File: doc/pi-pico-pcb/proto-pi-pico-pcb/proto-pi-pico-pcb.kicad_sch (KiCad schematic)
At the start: 10 parts

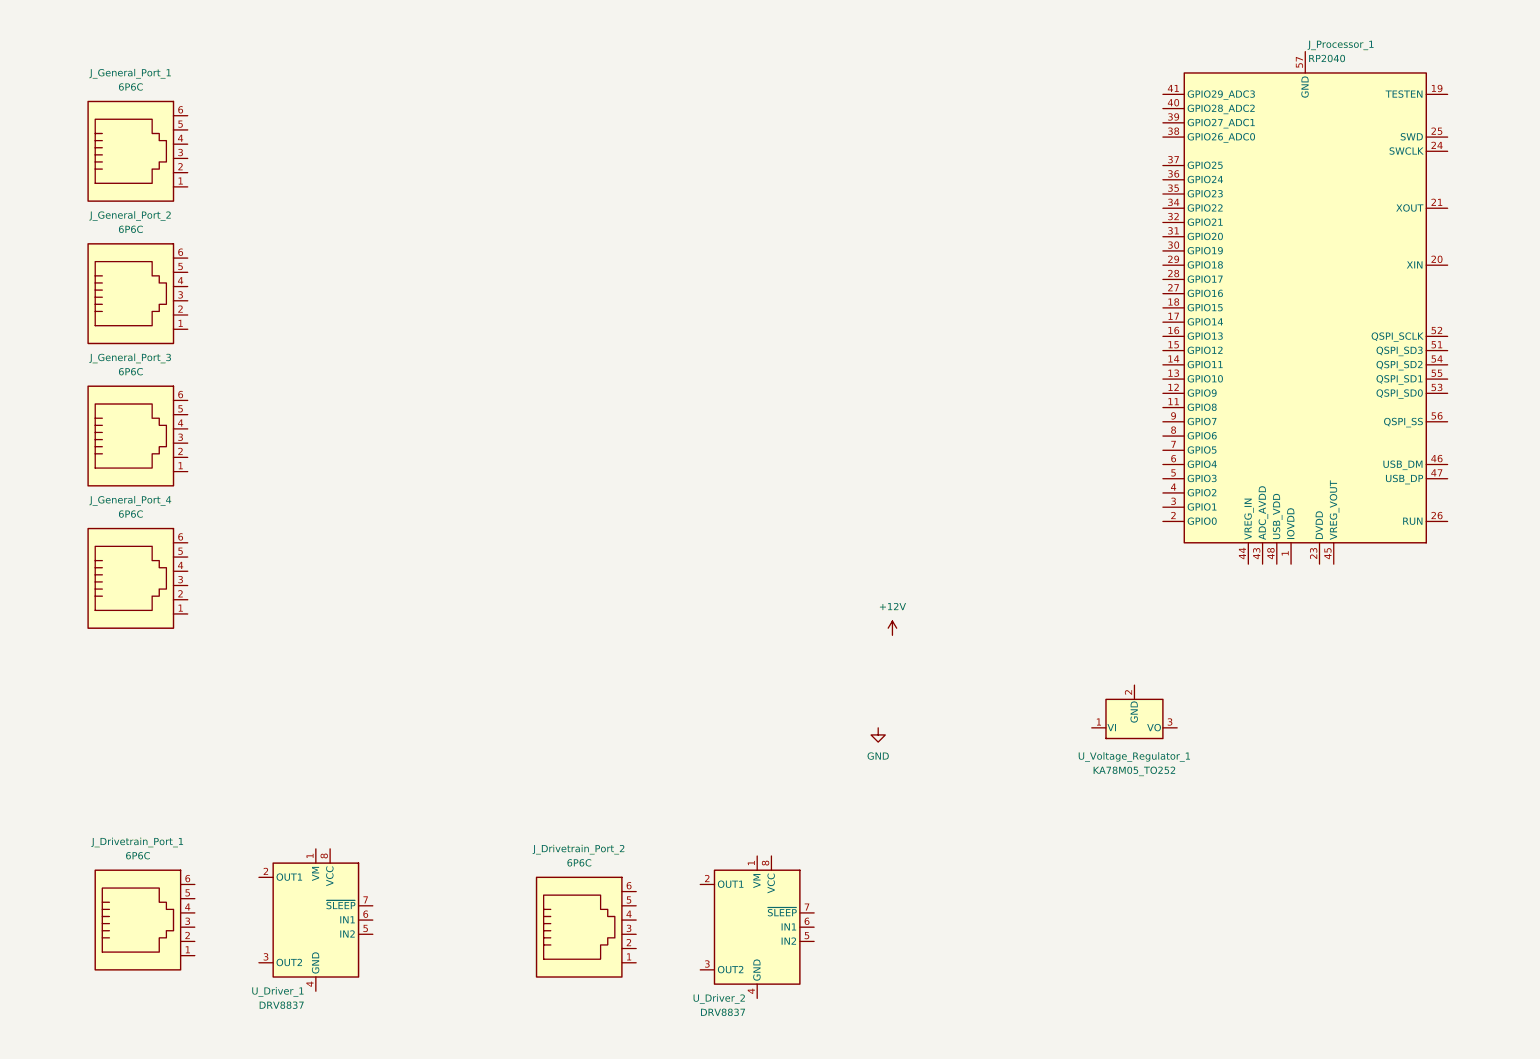
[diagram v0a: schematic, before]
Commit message: added grounds
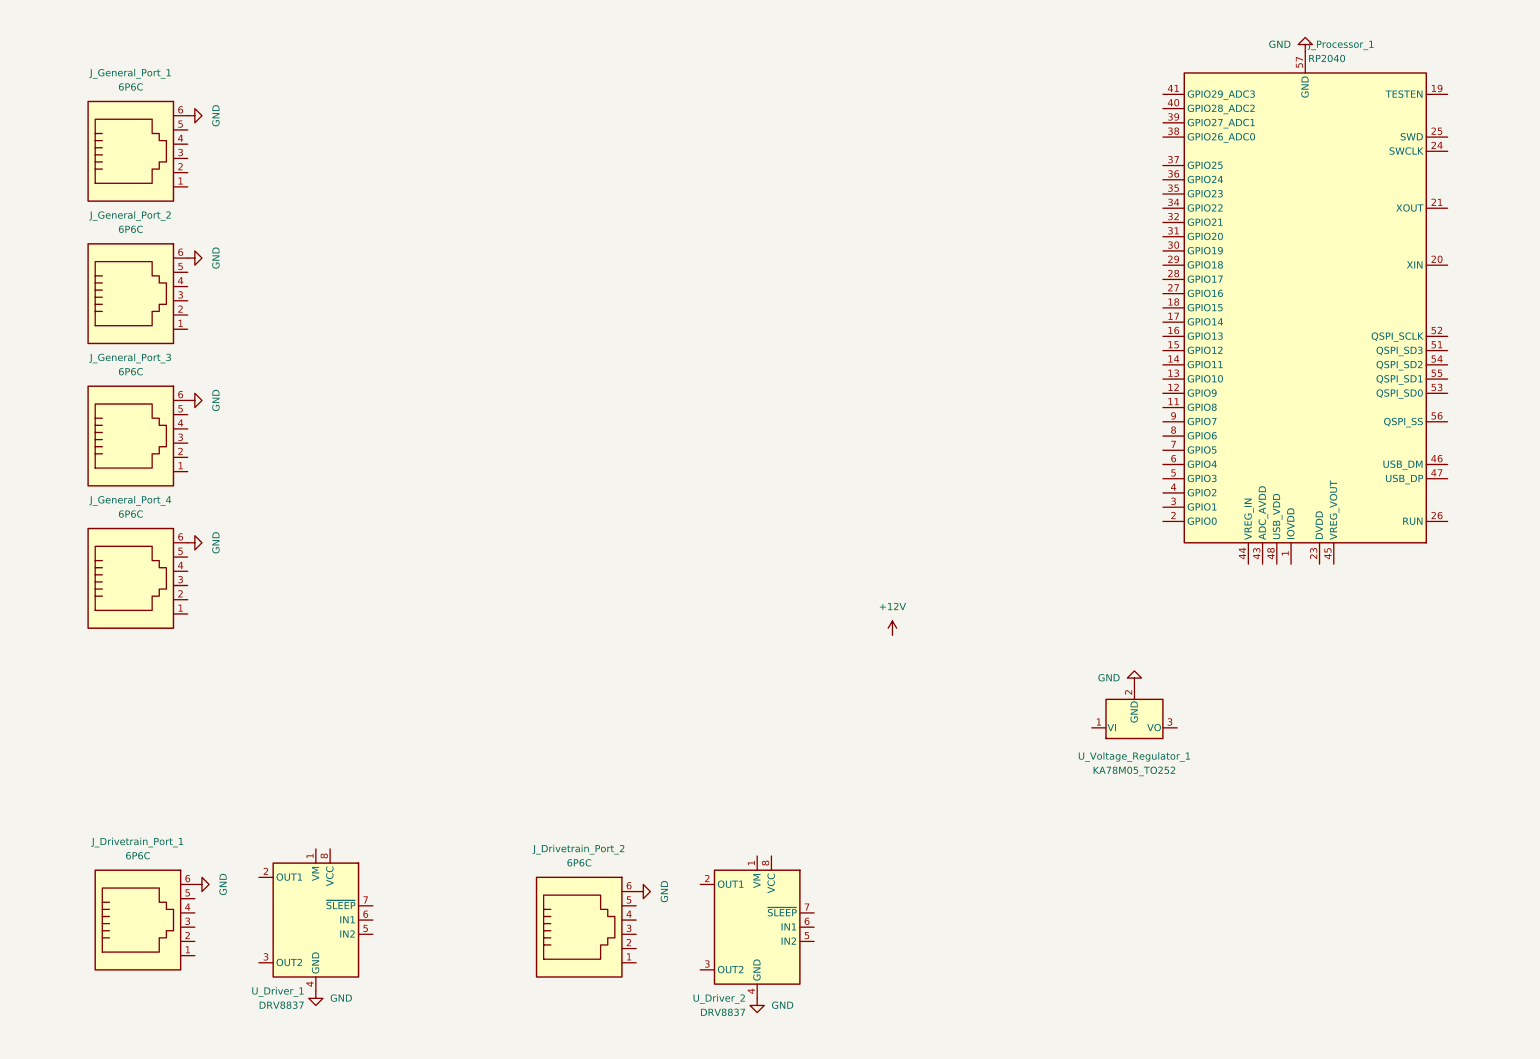
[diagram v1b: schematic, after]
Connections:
- net GND: now also J_Drivetrain_Port_1.6, J_Drivetrain_Port_2.6, J_General_Port_1.6, J_General_Port_2.6, J_General_Port_3.6, J_General_Port_4.6, J_Processor_1.57 (GND), U_Driver_1.4 (GND), U_Driver_1.9 (GND), U_Driver_2.4 (GND), U_Driver_2.9 (GND), U_Voltage_Regulator_1.2 (GND)
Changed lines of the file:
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@@
 (kicad_sch (version 20211123) (generator eeschema)
   (paper "A4")
+  (symbol (lib_id "power:GND") (at 46.99 107.95 90) (unit 1)
+    (in_bom yes) (on_board yes) (fields_autoplaced)
+    (property "Reference" "#PWR?" (id 0) (at 53.34 107.95 0)
+      (effects (font (size 1.27 1.27)) hide)
+    )
+    (property "Value" "GND" (id 1) (at 52.07 107.95 0))
+    (property "Footprint" "" (id 2) (at 46.99 107.95 0)
+      (effects (font (size 1.27 1.27)) hide)
+    )
+    (property "Datasheet" "" (id 3) (at 46.99 107.95 0)
+      (effects (font (size 1.27 1.27)) hide)
+    )
+    (pin "1")
+  )
   (symbol (lib_id "Connector:6P6C") (at 36.83 39.37 0) (unit 1)
     (in_bom yes) (on_board yes) (fields_autoplaced)
@@
     (pin "6")
   )
+  (symbol (lib_id "power:GND") (at 48.26 168.91 90) (unit 1)
+    (in_bom yes) (on_board yes) (fields_autoplaced)
+    (property "Reference" "#PWR?" (id 0) (at 54.61 168.91 0)
+      (effects (font (size 1.27 1.27)) hide)
+    )
+    (property "Value" "GND" (id 1) (at 53.34 168.91 0))
+    (property "Footprint" "" (id 2) (at 48.26 168.91 0)
+      (effects (font (size 1.27 1.27)) hide)
+    )
+    (property "Datasheet" "" (id 3) (at 48.26 168.91 0)
+      (effects (font (size 1.27 1.27)) hide)
+    )
+    (pin "1")
+  )
   (symbol (lib_id "power:+12V") (at 172.72 124.46 0) (unit 1)
     (in_bom yes) (on_board yes) (fields_autoplaced)
@@
     )
     (property "Datasheet" "" (id 3) (at 172.72 124.46 0)
+      (effects (font (size 1.27 1.27)) hide)
+    )
+    (pin "1")
+  )
+  (symbol (lib_id "power:GND") (at 246.38 20.32 0) (mirror x) (unit 1)
+    (in_bom yes) (on_board yes) (fields_autoplaced)
+    (property "Reference" "#PWR?" (id 0) (at 246.38 13.97 0)
+      (effects (font (size 1.27 1.27)) hide)
+    )
+    (property "Value" "GND" (id 1) (at 243.84 19.0499 0)
+      (effects (font (size 1.27 1.27)) (justify right))
+    )
+    (property "Footprint" "" (id 2) (at 246.38 20.32 0)
+      (effects (font (size 1.27 1.27)) hide)
+    )
+    (property "Datasheet" "" (id 3) (at 246.38 20.32 0)
+      (effects (font (size 1.27 1.27)) hide)
+    )
+    (pin "1")
+  )
+  (symbol (lib_id "power:GND") (at 148.59 189.23 0) (unit 1)
+    (in_bom yes) (on_board yes) (fields_autoplaced)
+    (property "Reference" "#PWR?" (id 0) (at 148.59 195.58 0)
+      (effects (font (size 1.27 1.27)) hide)
+    )
+    (property "Value" "GND" (id 1) (at 151.13 190.4999 0)
+      (effects (font (size 1.27 1.27)) (justify left))
+    )
+    (property "Footprint" "" (id 2) (at 148.59 189.23 0)
+      (effects (font (size 1.27 1.27)) hide)
+    )
+    (property "Datasheet" "" (id 3) (at 148.59 189.23 0)
+      (effects (font (size 1.27 1.27)) hide)
+    )
+    (pin "1")
+  )
+  (symbol (lib_id "power:GND") (at 69.85 187.96 0) (unit 1)
+    (in_bom yes) (on_board yes) (fields_autoplaced)
+    (property "Reference" "#PWR?" (id 0) (at 69.85 194.31 0)
+      (effects (font (size 1.27 1.27)) hide)
+    )
+    (property "Value" "GND" (id 1) (at 72.39 189.2299 0)
+      (effects (font (size 1.27 1.27)) (justify left))
+    )
+    (property "Footprint" "" (id 2) (at 69.85 187.96 0)
+      (effects (font (size 1.27 1.27)) hide)
+    )
+    (property "Datasheet" "" (id 3) (at 69.85 187.96 0)
       (effects (font (size 1.27 1.27)) hide)
     )
@@
     (pin "6")
   )
-  (symbol (lib_id "power:GND") (at 170.18 140.97 0) (unit 1)
-    (in_bom yes) (on_board yes) (fields_autoplaced)
-    (property "Reference" "#PWR?" (id 0) (at 170.18 147.32 0)
-      (effects (font (size 1.27 1.27)) hide)
-    )
-    (property "Value" "GND" (id 1) (at 170.18 146.05 0))
-    (property "Footprint" "" (id 2) (at 170.18 140.97 0)
-      (effects (font (size 1.27 1.27)) hide)
-    )
-    (property "Datasheet" "" (id 3) (at 170.18 140.97 0)
+  (symbol (lib_id "power:GND") (at 46.99 57.15 90) (unit 1)
+    (in_bom yes) (on_board yes) (fields_autoplaced)
+    (property "Reference" "#PWR?" (id 0) (at 53.34 57.15 0)
+      (effects (font (size 1.27 1.27)) hide)
+    )
+    (property "Value" "GND" (id 1) (at 52.07 57.15 0))
+    (property "Footprint" "" (id 2) (at 46.99 57.15 0)
+      (effects (font (size 1.27 1.27)) hide)
+    )
+    (property "Datasheet" "" (id 3) (at 46.99 57.15 0)
+      (effects (font (size 1.27 1.27)) hide)
+    )
+    (pin "1")
+  )
+  (symbol (lib_id "power:GND") (at 46.99 31.75 90) (unit 1)
+    (in_bom yes) (on_board yes) (fields_autoplaced)
+    (property "Reference" "#PWR?" (id 0) (at 53.34 31.75 0)
+      (effects (font (size 1.27 1.27)) hide)
+    )
+    (property "Value" "GND" (id 1) (at 52.07 31.75 0))
+    (property "Footprint" "" (id 2) (at 46.99 31.75 0)
+      (effects (font (size 1.27 1.27)) hide)
+    )
+    (property "Datasheet" "" (id 3) (at 46.99 31.75 0)
+      (effects (font (size 1.27 1.27)) hide)
+    )
+    (pin "1")
+  )
+  (symbol (lib_id "power:GND") (at 46.99 82.55 90) (unit 1)
+    (in_bom yes) (on_board yes) (fields_autoplaced)
+    (property "Reference" "#PWR?" (id 0) (at 53.34 82.55 0)
+      (effects (font (size 1.27 1.27)) hide)
+    )
+    (property "Value" "GND" (id 1) (at 52.07 82.55 0))
+    (property "Footprint" "" (id 2) (at 46.99 82.55 0)
+      (effects (font (size 1.27 1.27)) hide)
+    )
+    (property "Datasheet" "" (id 3) (at 46.99 82.55 0)
+      (effects (font (size 1.27 1.27)) hide)
+    )
+    (pin "1")
+  )
+  (symbol (lib_id "power:GND") (at 215.9 133.35 0) (mirror x) (unit 1)
+    (in_bom yes) (on_board yes) (fields_autoplaced)
+    (property "Reference" "#PWR?" (id 0) (at 215.9 127 0)
+      (effects (font (size 1.27 1.27)) hide)
+    )
+    (property "Value" "GND" (id 1) (at 213.36 132.0799 0)
+      (effects (font (size 1.27 1.27)) (justify right))
+    )
+    (property "Footprint" "" (id 2) (at 215.9 133.35 0)
+      (effects (font (size 1.27 1.27)) hide)
+    )
+    (property "Datasheet" "" (id 3) (at 215.9 133.35 0)
       (effects (font (size 1.27 1.27)) hide)
     )
@@
     (pin "9")
   )
+  (symbol (lib_id "power:GND") (at 127 170.18 90) (unit 1)
+    (in_bom yes) (on_board yes) (fields_autoplaced)
+    (property "Reference" "#PWR?" (id 0) (at 133.35 170.18 0)
+      (effects (font (size 1.27 1.27)) hide)
+    )
+    (property "Value" "GND" (id 1) (at 132.08 170.18 0))
+    (property "Footprint" "" (id 2) (at 127 170.18 0)
+      (effects (font (size 1.27 1.27)) hide)
+    )
+    (property "Datasheet" "" (id 3) (at 127 170.18 0)
+      (effects (font (size 1.27 1.27)) hide)
+    )
+    (pin "1")
+  )
   (sheet_instances
     (path "/" (page "1"))
   )
   (symbol_instances
+    (path "/138cc681-f9fa-48fc-8e00-de4045d4db12"
+      (reference "#PWR?") (unit 1) (value "GND") (footprint "")
+    )
+    (path "/1a2c0c7b-84d6-435d-8df9-a2504ff435de"
+      (reference "#PWR?") (unit 1) (value "GND") (footprint "")
+    )
     (path "/264169b5-390b-4b92-9d98-e580f1b5ce2f"
       (reference "#PWR?") (unit 1) (value "+12V") (footprint "")
     )
-    (path "/84fc61f1-6984-4905-a3b6-da52e2be2902"
-      (reference "#PWR?") (unit 1) (value "GND") (footprint "")
-    )
+    (path "/2e064d7a-8023-4e51-96a6-e76a3b76efd4"
+      (reference "#PWR?") (unit 1) (value "GND") (footprint "")
+    )
+    (path "/2ef69f6d-c876-4731-bce7-335d389180a6"
+      (reference "#PWR?") (unit 1) (value "GND") (footprint "")
+    )
+    (path "/3c540014-67b7-4b2f-9471-77b98f9b09d4"
+      (reference "#PWR?") (unit 1) (value "GND") (footprint "")
+    )
+    (path "/6e2778d5-7e9c-4653-b34b-aeefc29d6081"
+      (reference "#PWR?") (unit 1) (value "GND") (footprint "")
+    )
+    (path "/70398b98-b220-456d-8ed9-c06847a72d5d"
+      (reference "#PWR?") (unit 1) (value "GND") (footprint "")
+    )
+    (path "/747bb9af-c04f-46d6-b328-e44f90ffd5b8"
+      (reference "#PWR?") (unit 1) (value "GND") (footprint "")
+    )
+    (path "/a4790439-3952-431f-bcaa-1d0fbdcef256"
+      (reference "#PWR?") (unit 1) (value "GND") (footprint "")
+    )
+    (path "/fca40407-5290-471e-8c74-b9cdff750289"
+      (reference "#PWR?") (unit 1) (value "GND") (footprint "")
+    )

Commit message: added bypass capacitors
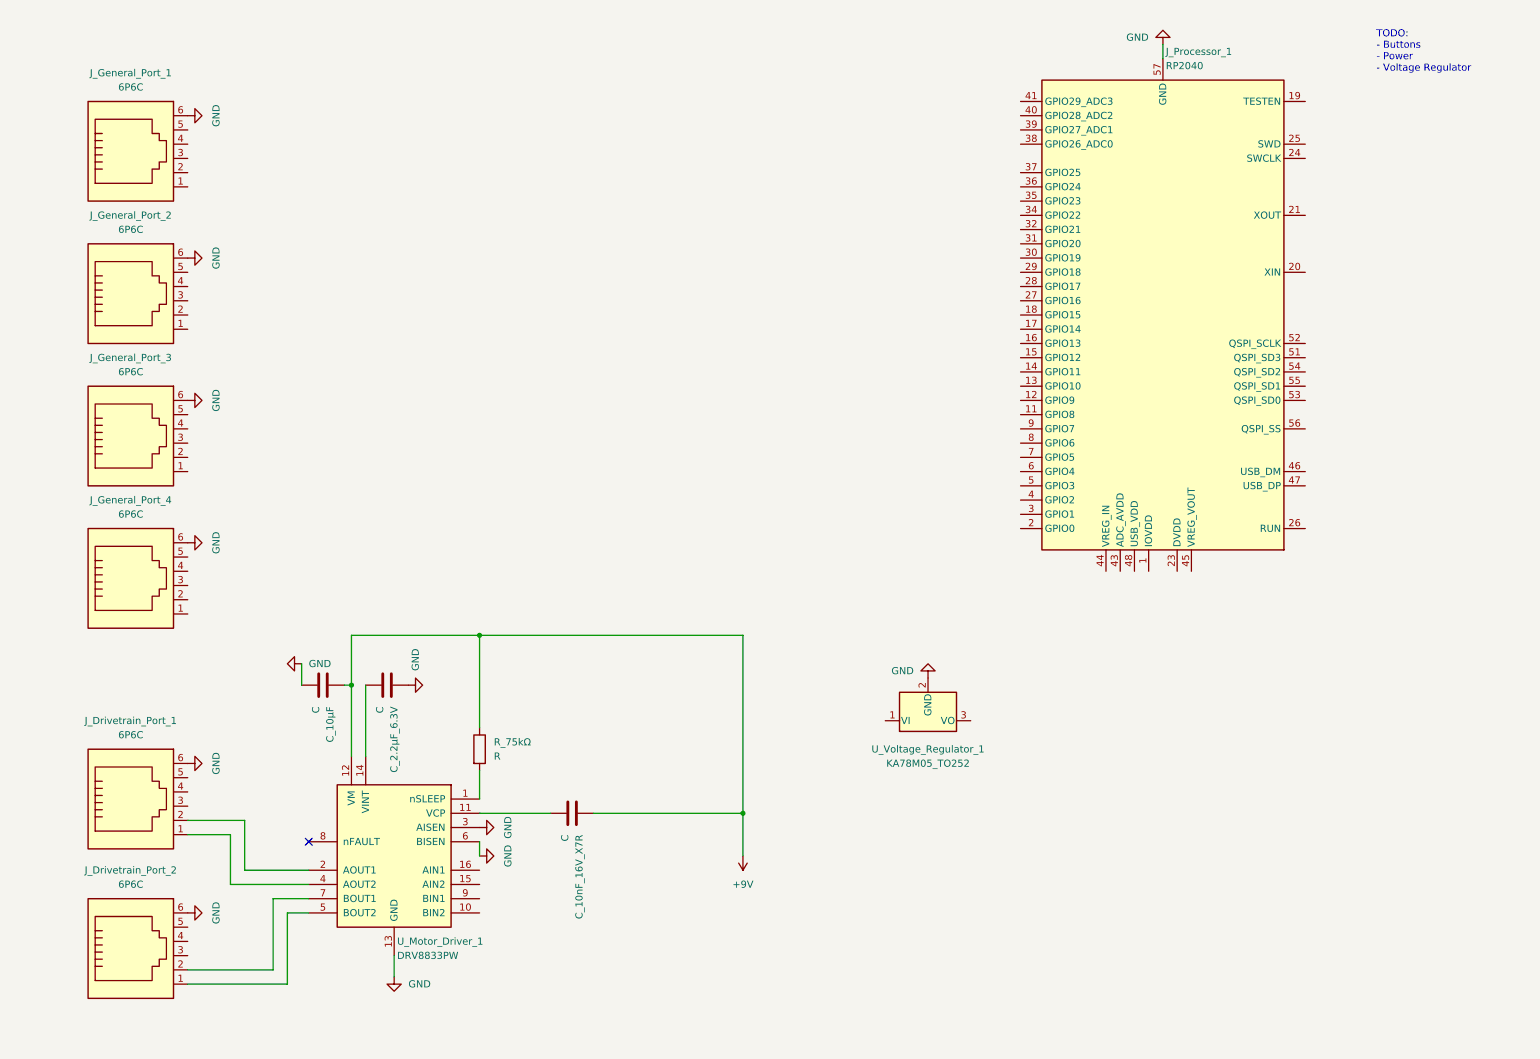
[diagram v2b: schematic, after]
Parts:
- removed U_Driver_1, U_Driver_2: DRV8837, Package_SON:WSON-8-1EP_2x2mm_P0.5mm_EP0.9x1.6mm, symbol Driver_Motor:DRV8837
- added C_10nF_16V_X7R, C_10μF, C_2.2μF_6.3V: C, symbol Device:C
- added R_75kΩ: R, symbol Device:R
- added U_Motor_Driver_1: DRV8833PW, Package_SO:TSSOP-16_4.4x5mm_P0.65mm, symbol Driver_Motor:DRV8833PW
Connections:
- net GND: now also C_10μF.2, C_2.2μF_6.3V.1, U_Motor_Driver_1.13 (GND), U_Motor_Driver_1.3 (AISEN), U_Motor_Driver_1.6 (BISEN)
- net at J_Drivetrain_Port_1.1: now also U_Motor_Driver_1.4 (AOUT2)
- net at J_Drivetrain_Port_1.2: now also U_Motor_Driver_1.2 (AOUT1)
- net at J_Drivetrain_Port_2.1: now also U_Motor_Driver_1.5 (BOUT2)
- net at J_Drivetrain_Port_2.2: now also U_Motor_Driver_1.7 (BOUT1)
- new net: R_75kΩ.2, U_Motor_Driver_1.1 (nSLEEP)
- new net: C_10nF_16V_X7R.2, U_Motor_Driver_1.11 (VCP)
- new net: C_2.2μF_6.3V.2, U_Motor_Driver_1.14 (VINT)
- new net +9V: C_10nF_16V_X7R.1, C_10μF.1, R_75kΩ.1, U_Motor_Driver_1.12 (VM)
- no-connect marks 0 -> 1
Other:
- note added: "TODO: - Buttons - Power - Voltage Regulator"
- moved on the sheet: J_Drivetrain_Port_1, J_Drivetrain_Port_2, J_Processor_1, U_Voltage_Regulator_1
